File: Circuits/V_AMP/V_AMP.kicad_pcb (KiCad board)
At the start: 2 copper layers, 103.5 x 153.8 mm, 138 parts, among them P1 INPUT, P2 GAIN_ADJ, P3 OUTPUT (0-5V), P4 POWER, U1 OPA277, U2 LM393, U3 OPA277

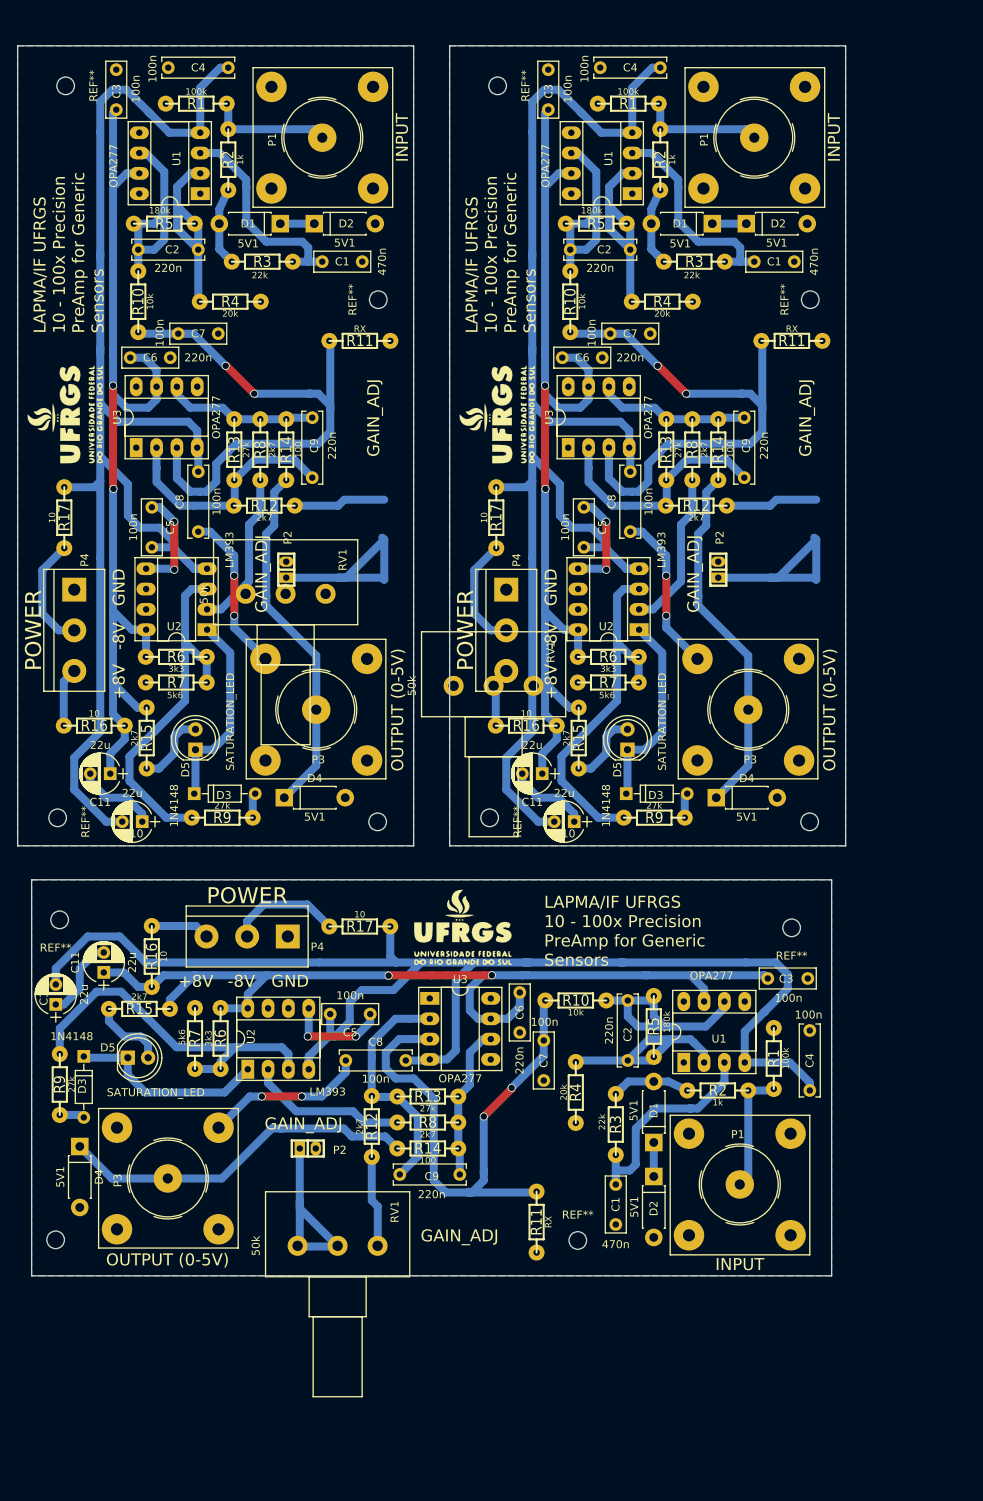
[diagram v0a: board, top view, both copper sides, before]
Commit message: EDIT: Shunt power resistors for alimentation input
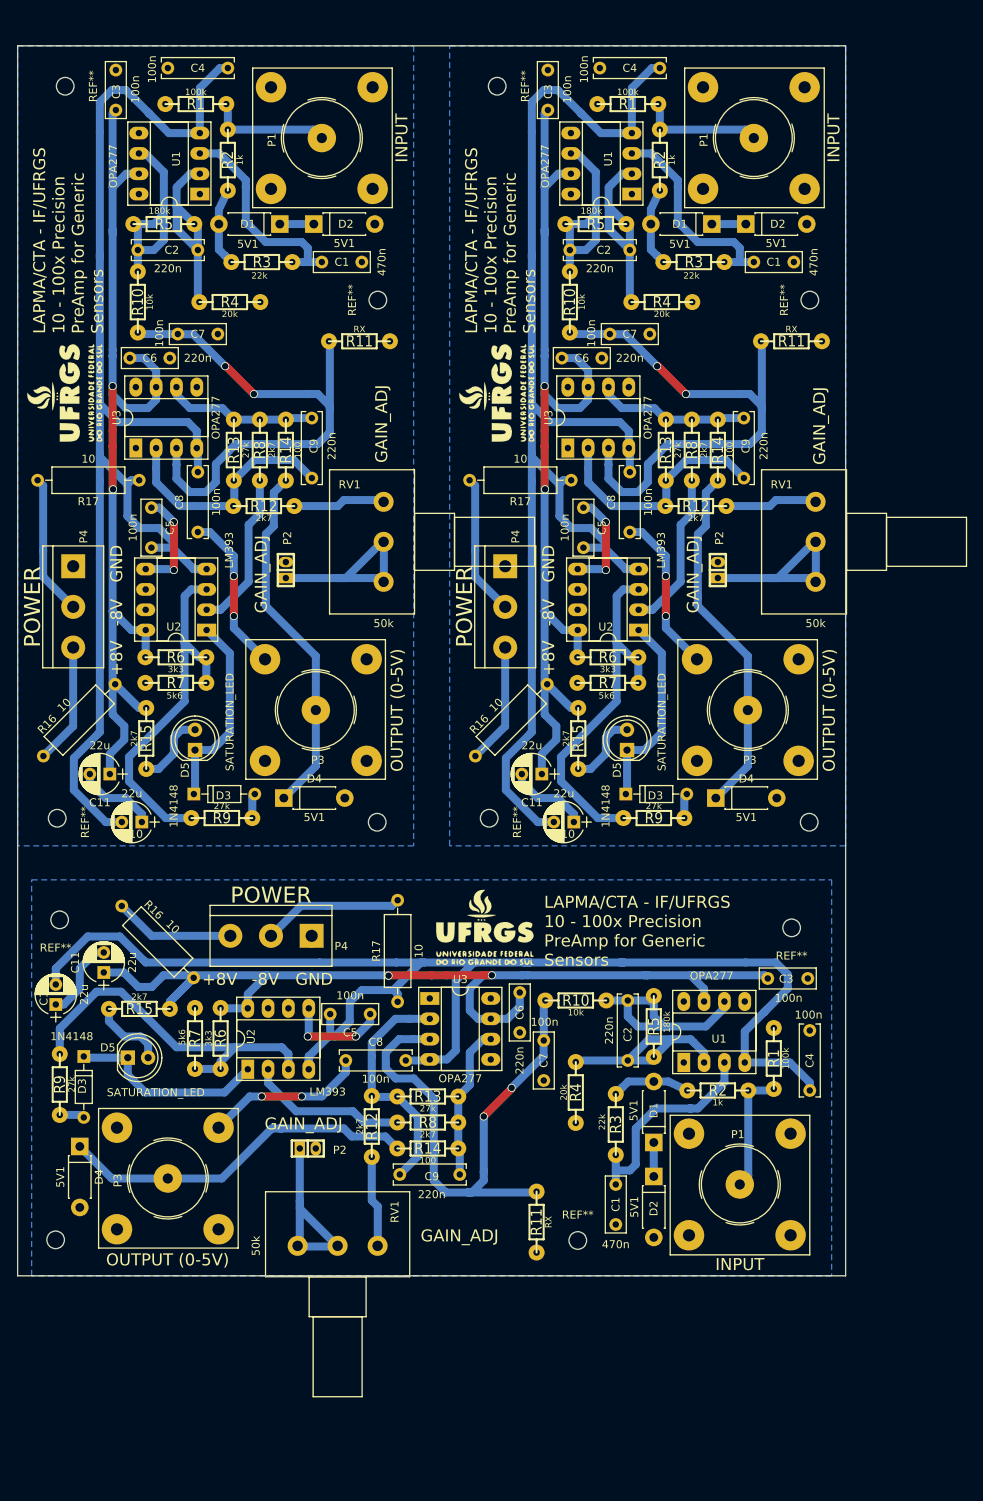
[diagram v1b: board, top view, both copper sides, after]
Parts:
- removed the C1 at (142.3, 59.7)
- removed the C1 at (88.3, 59.7)
- removed the C10 at (119.8, 129.7)
- removed the C10 at (65.8, 129.7)
- removed the C11 at (115.8, 123.7)
- removed the C11 at (61.8, 123.7)
- removed the C2 at (119.3, 58.2)
- removed the C2 at (65.3, 58.2)
- removed the C3 at (116.6, 35.7)
- removed the C3 at (62.6, 35.7)
- removed the C4 at (123.1, 35.5)
- removed the C4 at (69.1, 35.5)
- removed the C5 at (121.0, 90.4)
- removed the C5 at (67.0, 90.4)
- removed the C6 at (123.3, 71.7)
- removed the C6 at (69.3, 71.7)
- removed the C7 at (129.3, 68.7)
- removed the C7 at (75.3, 68.7)
- removed the C8 at (126.8, 93.5)
- removed the C8 at (72.8, 93.5)
- removed the C9 at (141.1, 86.7)
- removed the C9 at (87.1, 86.7)
- removed the D1 at (137.1, 55.0)
- removed the D1 at (83.1, 55.0)
- removed the D2 at (141.3, 55.0)
- removed the D2 at (87.3, 55.0)
- removed the D3 at (126.3, 126.2)
- removed the D3 at (72.3, 126.2)
- removed the D4 at (137.6, 126.7)
- removed the D4 at (83.6, 126.7)
- removed the D5 at (126.5, 120.7)
- removed the D5 at (72.5, 120.7)
- removed the G*** at (110.2, 78.8)
- removed the G*** at (56.2, 78.8)
- removed the P1 at (142.3, 44.2)
- removed the P1 at (88.3, 44.2)
- removed the P2 at (137.8, 98.2)
- removed the P2 at (83.8, 98.2)
- removed the P3 at (141.6, 115.7)
- removed the P3 at (87.6, 115.7)
- removed the P4 at (111.3, 100.7)
- removed the P4 at (57.3, 100.7)
- removed the R1 at (126.6, 40.0)
- removed the R1 at (72.6, 40.0)
- removed the R10 at (119.3, 64.7)
- removed the R10 at (65.3, 64.7)
- removed the R11 at (147.0, 69.6)
- removed the R11 at (93.0, 69.6)
- removed the R12 at (135.1, 90.2)
- removed the R12 at (81.1, 90.2)
- removed the R13 at (131.3, 83.2)
- removed the R13 at (77.3, 83.2)
- removed the R14 at (137.8, 83.2)
- removed the R14 at (83.8, 83.2)
- removed the R15 at (120.4, 119.3)
- removed the R15 at (66.4, 119.3)
- removed the R16 at (113.8, 117.7)
- removed the R16 at (59.8, 117.7)
- removed the R17 at (110.1, 91.7)
- removed the R17 at (56.1, 91.7)
- removed the R2 at (130.6, 47.0)
- removed the R2 at (76.6, 47.0)
- removed the R3 at (134.8, 59.7)
- removed the R3 at (80.8, 59.7)
- removed the R4 at (130.8, 64.7)
- removed the R4 at (76.8, 64.7)
- removed the R5 at (122.6, 55.0)
- removed the R5 at (68.6, 55.0)
- removed the R6 at (124.1, 109.1)
- removed the R6 at (70.1, 109.1)
- removed the R7 at (124.1, 112.3)
- removed the R7 at (70.1, 112.3)
- removed the R8 at (134.6, 83.2)
- removed the R8 at (80.6, 83.2)
- removed the R9 at (129.8, 129.2)
- removed the R9 at (75.8, 129.2)
- removed the REF** at (110.2, 37.8)
- removed the REF** at (149.3, 64.5)
- removed the REF** at (149.2, 129.8)
- removed the REF** at (109.2, 129.2)
- removed the REF** at (55.2, 129.2)
- removed the REF** at (95.2, 129.8)
- removed the REF** at (95.3, 64.5)
- removed the REF** at (56.2, 37.8)
- removed the RV1 at (104.8, 112.8)
- removed the RV1 at (78.8, 101.2)
- removed the U1 at (127.1, 51.2)
- removed the U1 at (73.1, 51.2)
- removed the U2 at (127.9, 105.7)
- removed the U2 at (73.9, 105.7)
- removed the U3 at (119.1, 83.0)
- removed the U3 at (65.1, 83.0)
- added C1: 470n, Capacitors_THT:C_Rect_L7.0mm_W2.5mm_P5.00mm, F.Cu at (88.3, 59.8)
- added C1: 470n, Capacitors_THT:C_Rect_L7.0mm_W2.5mm_P5.00mm, F.Cu at (142.3, 59.8)
- added C10: 22u, Capacitors_THT:CP_Radial_D5.0mm_P2.50mm, F.Cu at (65.8, 129.8)
- added C10: 22u, Capacitors_THT:CP_Radial_D5.0mm_P2.50mm, F.Cu at (119.8, 129.8)
- added C11: 22u, Capacitors_THT:CP_Radial_D5.0mm_P2.50mm, F.Cu at (61.8, 123.8)
- added C11: 22u, Capacitors_THT:CP_Radial_D5.0mm_P2.50mm, F.Cu at (115.8, 123.8)
- added C2: 220n, Capacitors_THT:C_Rect_L9.0mm_W2.5mm_P7.50mm_MKT, F.Cu at (65.3, 58.3)
- added C2: 220n, Capacitors_THT:C_Rect_L9.0mm_W2.5mm_P7.50mm_MKT, F.Cu at (119.3, 58.3)
- added C3: 100n, Capacitors_THT:C_Rect_L7.0mm_W2.5mm_P5.00mm, F.Cu at (62.5, 35.8)
- added C3: 100n, Capacitors_THT:C_Rect_L7.0mm_W2.5mm_P5.00mm, F.Cu at (116.5, 35.8)
- added C4: 100n, Capacitors_THT:C_Rect_L9.0mm_W2.5mm_P7.50mm_MKT, F.Cu at (69.0, 35.5)
- added C4: 100n, Capacitors_THT:C_Rect_L9.0mm_W2.5mm_P7.50mm_MKT, F.Cu at (123.0, 35.5)
- added C5: 100n, Capacitors_THT:C_Rect_L7.0mm_W2.5mm_P5.00mm, F.Cu at (67.0, 90.5)
- added C5: 100n, Capacitors_THT:C_Rect_L7.0mm_W2.5mm_P5.00mm, F.Cu at (121.0, 90.5)
- added C6: 100n, Capacitors_THT:C_Rect_L7.0mm_W2.5mm_P5.00mm, F.Cu at (69.3, 71.8)
- added C6: 100n, Capacitors_THT:C_Rect_L7.0mm_W2.5mm_P5.00mm, F.Cu at (123.3, 71.8)
- added C7: 220n, Capacitors_THT:C_Rect_L7.0mm_W2.5mm_P5.00mm, F.Cu at (75.3, 68.8)
- added C7: 220n, Capacitors_THT:C_Rect_L7.0mm_W2.5mm_P5.00mm, F.Cu at (129.3, 68.8)
- added C8: 100n, Capacitors_THT:C_Rect_L9.0mm_W2.5mm_P7.50mm_MKT, F.Cu at (72.8, 93.5)
- added C8: 100n, Capacitors_THT:C_Rect_L9.0mm_W2.5mm_P7.50mm_MKT, F.Cu at (126.8, 93.5)
- added C9: 220n, Capacitors_THT:C_Rect_L9.0mm_W2.5mm_P7.50mm_MKT, F.Cu at (87.0, 86.8)
- added C9: 220n, Capacitors_THT:C_Rect_L9.0mm_W2.5mm_P7.50mm_MKT, F.Cu at (141.0, 86.8)
- added D1: 5V1, Diodes_THT:D_DO-41_SOD81_P7.62mm_Horizontal, F.Cu at (83.0, 55.0)
- added D1: 5V1, Diodes_THT:D_DO-41_SOD81_P7.62mm_Horizontal, F.Cu at (137.0, 55.0)
- added D2: 5V1, Diodes_THT:D_DO-41_SOD81_P7.62mm_Horizontal, F.Cu at (87.3, 55.0)
- added D2: 5V1, Diodes_THT:D_DO-41_SOD81_P7.62mm_Horizontal, F.Cu at (141.3, 55.0)
- added D3: 1N4148, Diodes_THT:D_DO-35_SOD27_P7.62mm_Horizontal, F.Cu at (72.3, 126.3)
- added D3: 1N4148, Diodes_THT:D_DO-35_SOD27_P7.62mm_Horizontal, F.Cu at (126.3, 126.3)
- added D4: 5V1, Diodes_THT:D_DO-41_SOD81_P7.62mm_Horizontal, F.Cu at (83.5, 126.8)
- added D4: 5V1, Diodes_THT:D_DO-41_SOD81_P7.62mm_Horizontal, F.Cu at (137.5, 126.8)
- added D5: SATURATION_LED, LEDs:LED_D5.0mm, F.Cu at (72.4, 120.8)
- added D5: SATURATION_LED, LEDs:LED_D5.0mm, F.Cu at (126.4, 120.8)
- added G***: LOGO, Symbols:ufrgs, F.Cu at (56.2, 76.0)
- added G***: LOGO, Symbols:ufrgs, F.Cu at (110.2, 76.0)
- added P1: INPUT, Connectors:bnc-ci, F.Cu at (88.3, 44.3)
- added P1: INPUT, Connectors:bnc-ci, F.Cu at (142.3, 44.3)
- added P2: GAIN_ADJ, w_pin_strip:pin_strip_2mm_2, F.Cu at (83.8, 98.3)
- added P2: GAIN_ADJ, w_pin_strip:pin_strip_2mm_2, F.Cu at (137.8, 98.3)
- added P3: OUTPUT (0-5V), Connectors:bnc-ci, F.Cu at (87.5, 115.8)
- added P3: OUTPUT (0-5V), Connectors:bnc-ci, F.Cu at (141.5, 115.8)
- added P4: POWER, Connectors:bornier3, F.Cu at (57.2, 97.8)
- added P4: POWER, Connectors:bornier3, F.Cu at (111.2, 97.8)
- added R1: 100k, w_pth_resistors:RC03, F.Cu at (72.5, 40.0)
- added R1: 100k, w_pth_resistors:RC03, F.Cu at (126.5, 40.0)
- added R10: 10k, w_pth_resistors:RC03, F.Cu at (65.3, 64.8)
- added R10: 10k, w_pth_resistors:RC03, F.Cu at (119.3, 64.8)
- added R11: RX, w_pth_resistors:RC03, F.Cu at (93.0, 69.7)
- added R11: RX, w_pth_resistors:RC03, F.Cu at (147.0, 69.7)
- added R12: 2k7, w_pth_resistors:RC03, F.Cu at (81.0, 90.3)
- added R12: 2k7, w_pth_resistors:RC03, F.Cu at (135.0, 90.3)
- added R13: 27k, w_pth_resistors:RC03, F.Cu at (77.3, 83.3)
- added R13: 27k, w_pth_resistors:RC03, F.Cu at (131.3, 83.3)
- added R14: 100, w_pth_resistors:RC03, F.Cu at (83.8, 83.3)
- added R14: 100, w_pth_resistors:RC03, F.Cu at (137.8, 83.3)
- added R15: 2k7, w_pth_resistors:RC03, F.Cu at (66.3, 119.3)
- added R15: 2k7, w_pth_resistors:RC03, F.Cu at (120.3, 119.3)
- added R16: 10, Resistors_THT:R_Axial_DIN0309_L9.0mm_D3.2mm_P12.70mm_Horizontal, F.Cu at (62.4, 112.5)
- added R16: 10, Resistors_THT:R_Axial_DIN0309_L9.0mm_D3.2mm_P12.70mm_Horizontal, F.Cu at (116.4, 112.5)
- added R17: 10, Resistors_THT:R_Axial_DIN0309_L9.0mm_D3.2mm_P12.70mm_Horizontal, F.Cu at (65.4, 87.0)
- added R17: 10, Resistors_THT:R_Axial_DIN0309_L9.0mm_D3.2mm_P12.70mm_Horizontal, F.Cu at (119.4, 87.0)
- added R2: 1k, w_pth_resistors:RC03, F.Cu at (76.5, 47.0)
- added R2: 1k, w_pth_resistors:RC03, F.Cu at (130.5, 47.0)
- added R3: 22k, w_pth_resistors:RC03, F.Cu at (80.8, 59.8)
- added R3: 22k, w_pth_resistors:RC03, F.Cu at (134.8, 59.8)
- added R4: 20k, w_pth_resistors:RC03, F.Cu at (76.8, 64.8)
- added R4: 20k, w_pth_resistors:RC03, F.Cu at (130.8, 64.8)
- added R5: 180k, w_pth_resistors:RC03, F.Cu at (68.5, 55.0)
- added R5: 180k, w_pth_resistors:RC03, F.Cu at (122.5, 55.0)
- added R6: 3k3, w_pth_resistors:RC03, F.Cu at (70.0, 109.2)
- added R6: 3k3, w_pth_resistors:RC03, F.Cu at (124.0, 109.2)
- added R7: 5k6, w_pth_resistors:RC03, F.Cu at (70.0, 112.4)
- added R7: 5k6, w_pth_resistors:RC03, F.Cu at (124.0, 112.4)
- added R8: 2k7, w_pth_resistors:RC03, F.Cu at (80.5, 83.3)
- added R8: 2k7, w_pth_resistors:RC03, F.Cu at (134.5, 83.3)
- added R9: 27k, w_pth_resistors:RC03, F.Cu at (75.8, 129.3)
- added R9: 27k, w_pth_resistors:RC03, F.Cu at (129.8, 129.3)
- added REF**: MountingHole_2.2mm_M2, Mounting_Holes:MountingHole_2.2mm_M2, F.Cu at (56.2, 37.8)
- added REF**: MountingHole_2.2mm_M2, Mounting_Holes:MountingHole_2.2mm_M2, F.Cu at (95.3, 64.5)
- added REF**: MountingHole_2.2mm_M2, Mounting_Holes:MountingHole_2.2mm_M2, F.Cu at (95.2, 129.8)
- added REF**: MountingHole_2.2mm_M2, Mounting_Holes:MountingHole_2.2mm_M2, F.Cu at (55.2, 129.3)
- added REF**: MountingHole_2.2mm_M2, Mounting_Holes:MountingHole_2.2mm_M2, F.Cu at (109.2, 129.3)
- added REF**: MountingHole_2.2mm_M2, Mounting_Holes:MountingHole_2.2mm_M2, F.Cu at (149.2, 129.8)
- added REF**: MountingHole_2.2mm_M2, Mounting_Holes:MountingHole_2.2mm_M2, F.Cu at (149.3, 64.5)
- added REF**: MountingHole_2.2mm_M2, Mounting_Holes:MountingHole_2.2mm_M2, F.Cu at (110.2, 37.8)
- added RV1: 50k, Potentiometers:Potentiometer_Alps_RK163_Single_Vertical, F.Cu at (96.0, 99.8)
- added RV1: 50k, Potentiometers:Potentiometer_Alps_RK163_Single_Vertical, F.Cu at (150.0, 99.8)
- added U1: OPA277, Housings_DIP:DIP-8_W7.62mm_Socket_LongPads, F.Cu at (73.0, 51.3)
- added U1: OPA277, Housings_DIP:DIP-8_W7.62mm_Socket_LongPads, F.Cu at (127.0, 51.3)
- added U2: LM393, Housings_DIP:DIP-8_W7.62mm_Socket_LongPads, F.Cu at (73.9, 105.8)
- added U2: LM393, Housings_DIP:DIP-8_W7.62mm_Socket_LongPads, F.Cu at (127.9, 105.8)
- added U3: OPA277, Housings_DIP:DIP-8_W7.62mm_Socket_LongPads, F.Cu at (65.0, 83.0)
- added U3: OPA277, Housings_DIP:DIP-8_W7.62mm_Socket_LongPads, F.Cu at (119.0, 83.0)
- R16, R17: footprint w_pth_resistors:RC03 -> Resistors_THT:R_Axial_DIN0309_L9.0mm_D3.2mm_P12.70mm_Horizontal
- moved R17 10.5 mm to (97.8, 152.2), turned to 90 degrees
- moved R16 5.87 mm to (72.2, 149.2), turned to 135 degrees
- moved P4 2.98 mm to (87.0, 144.0)
- moved G*** 2.75 mm to (108.8, 143.0)
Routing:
- net Net-(P4-Pad3): track 16.1 -> 46.7 mm
- net +8V: track 355.5 -> 366.1 mm
- net Net-(P4-Pad2): track 45.6 -> 56.0 mm
- net -8V: track 519.1 -> 509.7 mm
- net Net-(P2-Pad1): track 83.7 -> 76.3 mm
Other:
- outline, holes or cut-outs redrawn
- board text added: "LAPMA/CTA - IF/UFRGS 10 - 100x Precision PreAmp for Generic Sensors"
- board text removed: "LAPMA/IF UFRGS 10 - 100x Precision PreAmp for Generic Sensors"

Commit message: ADD: Complete Current Source SCH+PCB w/ Gerbers
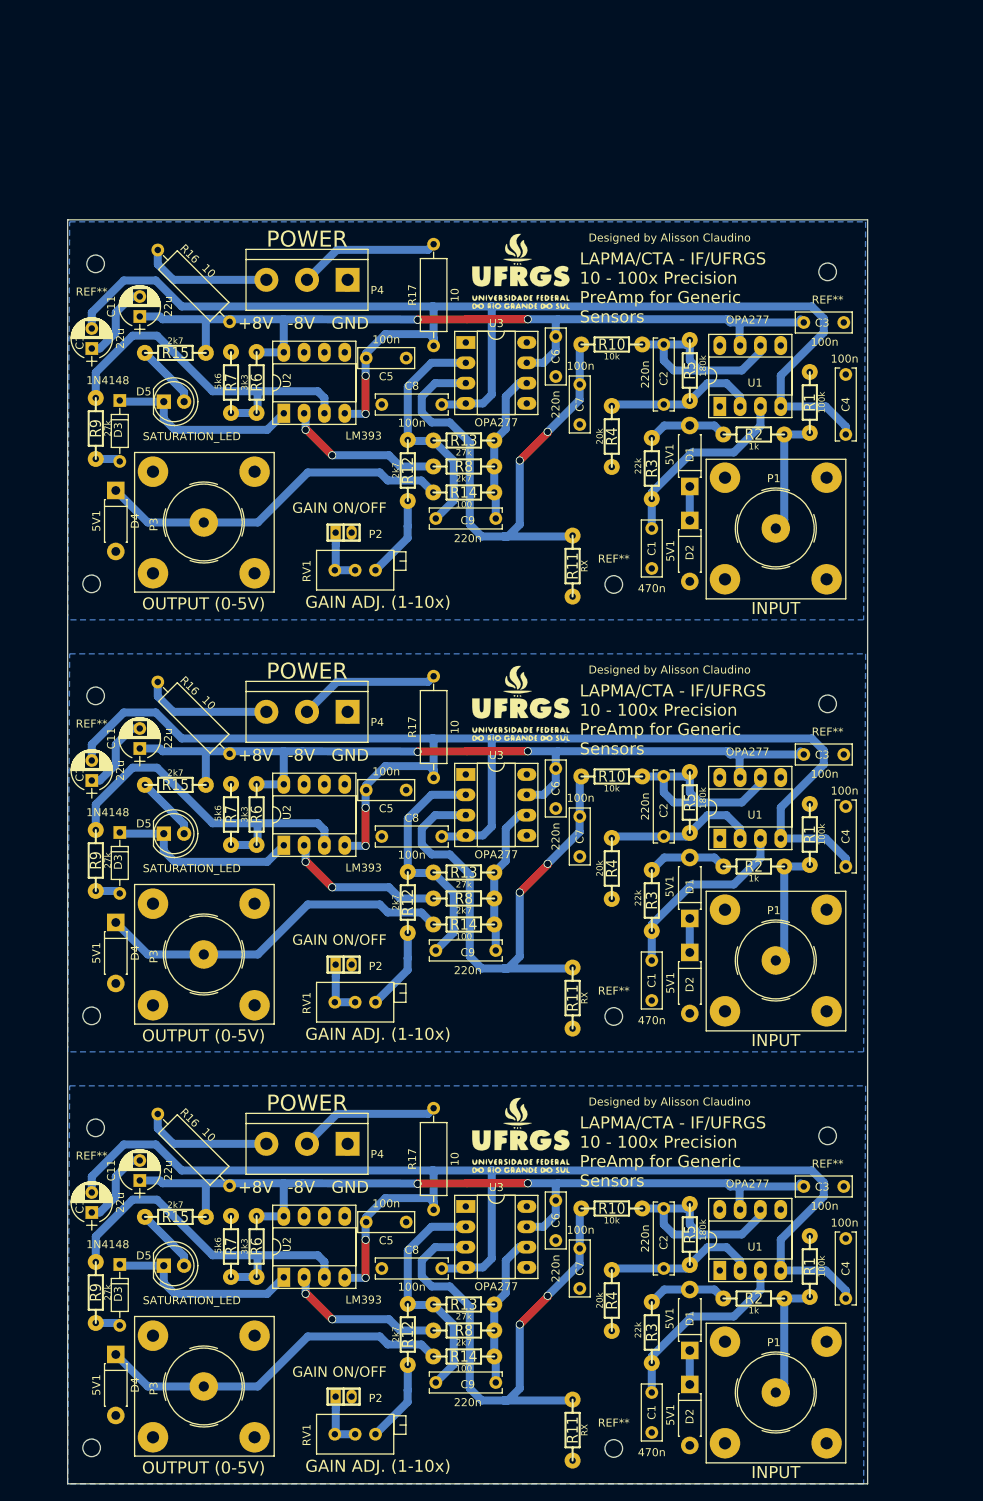
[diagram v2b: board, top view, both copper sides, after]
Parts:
- removed the C1 at (88.3, 59.8)
- removed the C1 at (142.3, 59.8)
- removed the C10 at (65.8, 129.8)
- removed the C10 at (119.8, 129.8)
- removed the C11 at (61.8, 123.8)
- removed the C11 at (115.8, 123.8)
- removed the C2 at (65.3, 58.3)
- removed the C2 at (119.3, 58.3)
- removed the C3 at (62.5, 35.8)
- removed the C3 at (116.5, 35.8)
- removed the C4 at (69.0, 35.5)
- removed the C4 at (123.0, 35.5)
- removed the C5 at (67.0, 90.5)
- removed the C5 at (121.0, 90.5)
- removed the C6 at (69.3, 71.8)
- removed the C6 at (123.3, 71.8)
- removed the C7 at (75.3, 68.8)
- removed the C7 at (129.3, 68.8)
- removed the C8 at (72.8, 93.5)
- removed the C8 at (126.8, 93.5)
- removed the C9 at (87.0, 86.8)
- removed the C9 at (141.0, 86.8)
- removed the D1 at (83.0, 55.0)
- removed the D1 at (137.0, 55.0)
- removed the D2 at (87.3, 55.0)
- removed the D2 at (141.3, 55.0)
- removed the D3 at (72.3, 126.3)
- removed the D3 at (126.3, 126.3)
- removed the D4 at (83.5, 126.8)
- removed the D4 at (137.5, 126.8)
- removed the D5 at (72.4, 120.8)
- removed the D5 at (126.4, 120.8)
- removed the G*** at (56.2, 76.0)
- removed the G*** at (110.2, 76.0)
- removed the P1 at (88.3, 44.3)
- removed the P1 at (142.3, 44.3)
- removed the P2 at (83.8, 98.3)
- removed the P2 at (137.8, 98.3)
- removed the P3 at (87.5, 115.8)
- removed the P3 at (141.5, 115.8)
- removed the P4 at (57.2, 97.8)
- removed the P4 at (111.2, 97.8)
- removed the R1 at (72.5, 40.0)
- removed the R1 at (126.5, 40.0)
- removed the R10 at (65.3, 64.8)
- removed the R10 at (119.3, 64.8)
- removed the R11 at (93.0, 69.7)
- removed the R11 at (147.0, 69.7)
- removed the R12 at (81.0, 90.3)
- removed the R12 at (135.0, 90.3)
- removed the R13 at (77.3, 83.3)
- removed the R13 at (131.3, 83.3)
- removed the R14 at (83.8, 83.3)
- removed the R14 at (137.8, 83.3)
- removed the R15 at (66.3, 119.3)
- removed the R15 at (120.3, 119.3)
- removed the R16 at (62.4, 112.5)
- removed the R16 at (116.4, 112.5)
- removed the R17 at (65.4, 87.0)
- removed the R17 at (119.4, 87.0)
- removed the R2 at (76.5, 47.0)
- removed the R2 at (130.5, 47.0)
- removed the R3 at (80.8, 59.8)
- removed the R3 at (134.8, 59.8)
- removed the R4 at (76.8, 64.8)
- removed the R4 at (130.8, 64.8)
- removed the R5 at (68.5, 55.0)
- removed the R5 at (122.5, 55.0)
- removed the R6 at (70.0, 109.2)
- removed the R6 at (124.0, 109.2)
- removed the R7 at (70.0, 112.4)
- removed the R7 at (124.0, 112.4)
- removed the R8 at (80.5, 83.3)
- removed the R8 at (134.5, 83.3)
- removed the R9 at (75.8, 129.3)
- removed the R9 at (129.8, 129.3)
- removed the REF** at (56.2, 37.8)
- removed the REF** at (95.3, 64.5)
- removed the REF** at (95.2, 129.8)
- removed the REF** at (55.2, 129.3)
- removed the REF** at (109.2, 129.3)
- removed the REF** at (149.2, 129.8)
- removed the REF** at (149.3, 64.5)
- removed the REF** at (110.2, 37.8)
- removed the RV1 at (96.0, 99.8)
- removed the RV1 at (150.0, 99.8)
- removed the U1 at (73.0, 51.3)
- removed the U1 at (127.0, 51.3)
- removed the U2 at (73.9, 105.8)
- removed the U2 at (127.9, 105.8)
- removed the U3 at (65.0, 83.0)
- removed the U3 at (119.0, 83.0)
- added C1: 470n, Capacitors_THT:C_Rect_L7.0mm_W2.5mm_P5.00mm, F.Cu at (129.5, 93.1)
- added C1: 470n, Capacitors_THT:C_Rect_L7.0mm_W2.5mm_P5.00mm, F.Cu at (129.5, 147.1)
- added C10: 22u, Capacitors_THT:CP_Radial_D5.0mm_P2.50mm, F.Cu at (59.5, 70.6)
- added C10: 22u, Capacitors_THT:CP_Radial_D5.0mm_P2.50mm, F.Cu at (59.5, 124.6)
- added C11: 22u, Capacitors_THT:CP_Radial_D5.0mm_P2.50mm, F.Cu at (65.5, 66.6)
- added C11: 22u, Capacitors_THT:CP_Radial_D5.0mm_P2.50mm, F.Cu at (65.5, 120.6)
- added C2: 220n, Capacitors_THT:C_Rect_L9.0mm_W2.5mm_P7.50mm_MKT, F.Cu at (131.0, 70.1)
- added C2: 220n, Capacitors_THT:C_Rect_L9.0mm_W2.5mm_P7.50mm_MKT, F.Cu at (131.0, 124.1)
- added C3: 100n, Capacitors_THT:C_Rect_L7.0mm_W2.5mm_P5.00mm, F.Cu at (153.5, 67.3)
- added C3: 100n, Capacitors_THT:C_Rect_L7.0mm_W2.5mm_P5.00mm, F.Cu at (153.5, 121.3)
- added C4: 100n, Capacitors_THT:C_Rect_L9.0mm_W2.5mm_P7.50mm_MKT, F.Cu at (153.8, 73.8)
- added C4: 100n, Capacitors_THT:C_Rect_L9.0mm_W2.5mm_P7.50mm_MKT, F.Cu at (153.8, 127.8)
- added C5: 100n, Capacitors_THT:C_Rect_L7.0mm_W2.5mm_P5.00mm, F.Cu at (98.8, 71.8)
- added C5: 100n, Capacitors_THT:C_Rect_L7.0mm_W2.5mm_P5.00mm, F.Cu at (98.8, 125.8)
- added C6: 100n, Capacitors_THT:C_Rect_L7.0mm_W2.5mm_P5.00mm, F.Cu at (117.5, 74.1)
- added C6: 100n, Capacitors_THT:C_Rect_L7.0mm_W2.5mm_P5.00mm, F.Cu at (117.5, 128.1)
- added C7: 220n, Capacitors_THT:C_Rect_L7.0mm_W2.5mm_P5.00mm, F.Cu at (120.5, 80.1)
- added C7: 220n, Capacitors_THT:C_Rect_L7.0mm_W2.5mm_P5.00mm, F.Cu at (120.5, 134.1)
- added C8: 100n, Capacitors_THT:C_Rect_L9.0mm_W2.5mm_P7.50mm_MKT, F.Cu at (95.8, 77.6)
- added C8: 100n, Capacitors_THT:C_Rect_L9.0mm_W2.5mm_P7.50mm_MKT, F.Cu at (95.8, 131.6)
- added C9: 220n, Capacitors_THT:C_Rect_L9.0mm_W2.5mm_P7.50mm_MKT, F.Cu at (102.5, 91.8)
- added C9: 220n, Capacitors_THT:C_Rect_L9.0mm_W2.5mm_P7.50mm_MKT, F.Cu at (102.5, 145.8)
- added D1: 5V1, Diodes_THT:D_DO-41_SOD81_P7.62mm_Horizontal, F.Cu at (134.3, 87.8)
- added D1: 5V1, Diodes_THT:D_DO-41_SOD81_P7.62mm_Horizontal, F.Cu at (134.3, 141.8)
- added D2: 5V1, Diodes_THT:D_DO-41_SOD81_P7.62mm_Horizontal, F.Cu at (134.3, 92.1)
- added D2: 5V1, Diodes_THT:D_DO-41_SOD81_P7.62mm_Horizontal, F.Cu at (134.3, 146.1)
- added D3: 1N4148, Diodes_THT:D_DO-35_SOD27_P7.62mm_Horizontal, F.Cu at (63.0, 77.1)
- added D3: 1N4148, Diodes_THT:D_DO-35_SOD27_P7.62mm_Horizontal, F.Cu at (63.0, 131.1)
- added D4: 5V1, Diodes_THT:D_DO-41_SOD81_P7.62mm_Horizontal, F.Cu at (62.5, 88.3)
- added D4: 5V1, Diodes_THT:D_DO-41_SOD81_P7.62mm_Horizontal, F.Cu at (62.5, 142.3)
- added D5: SATURATION_LED, LEDs:LED_D5.0mm, F.Cu at (68.5, 77.2)
- added D5: SATURATION_LED, LEDs:LED_D5.0mm, F.Cu at (68.5, 131.2)
- added G***: LOGO, Symbols:ufrgs, F.Cu at (113.2, 61.0)
- added G***: LOGO, Symbols:ufrgs, F.Cu at (113.2, 115.0)
- added P1: INPUT, Connectors:bnc-ci, F.Cu at (145.0, 93.1)
- added P1: INPUT, Connectors:bnc-ci, F.Cu at (145.0, 147.1)
- added P2: GAIN ON/OFF, w_pin_strip:pin_strip_2mm_2, F.Cu at (91.0, 93.6)
- added P2: GAIN ON/OFF, w_pin_strip:pin_strip_2mm_2, F.Cu at (91.0, 147.6)
- added P3: OUTPUT (0-5V), Connectors:bnc-ci, F.Cu at (73.5, 92.3)
- added P3: OUTPUT (0-5V), Connectors:bnc-ci, F.Cu at (73.5, 146.3)
- added P4: POWER, Connectors:bornier3, F.Cu at (91.5, 62.0)
- added P4: POWER, Connectors:bornier3, F.Cu at (91.5, 116.0)
- added R1: 100k, w_pth_resistors:RC03, F.Cu at (149.3, 77.3)
- added R1: 100k, w_pth_resistors:RC03, F.Cu at (149.3, 131.3)
- added R10: 10k, w_pth_resistors:RC03, F.Cu at (124.5, 70.1)
- added R10: 10k, w_pth_resistors:RC03, F.Cu at (124.5, 124.1)
- added R11: RX, w_pth_resistors:RC03, F.Cu at (119.6, 97.8)
- added R11: RX, w_pth_resistors:RC03, F.Cu at (119.6, 151.8)
- added R12: 2k7, w_pth_resistors:RC03, F.Cu at (99.0, 85.8)
- added R12: 2k7, w_pth_resistors:RC03, F.Cu at (99.0, 139.8)
- added R13: 27k, w_pth_resistors:RC03, F.Cu at (106.0, 82.1)
- added R13: 27k, w_pth_resistors:RC03, F.Cu at (106.0, 136.1)
- added R14: 100, w_pth_resistors:RC03, F.Cu at (106.0, 88.6)
- added R14: 100, w_pth_resistors:RC03, F.Cu at (106.0, 142.6)
- added R15: 2k7, w_pth_resistors:RC03, F.Cu at (70.0, 71.1)
- added R15: 2k7, w_pth_resistors:RC03, F.Cu at (70.0, 125.1)
- added R16: 10, Resistors_THT:R_Axial_DIN0309_L9.0mm_D3.2mm_P12.70mm_Horizontal, F.Cu at (76.8, 67.2)
- added R16: 10, Resistors_THT:R_Axial_DIN0309_L9.0mm_D3.2mm_P12.70mm_Horizontal, F.Cu at (76.8, 121.2)
- added R17: 10, Resistors_THT:R_Axial_DIN0309_L9.0mm_D3.2mm_P12.70mm_Horizontal, F.Cu at (102.2, 70.2)
- added R17: 10, Resistors_THT:R_Axial_DIN0309_L9.0mm_D3.2mm_P12.70mm_Horizontal, F.Cu at (102.2, 124.2)
- added R2: 1k, w_pth_resistors:RC03, F.Cu at (142.3, 81.3)
- added R2: 1k, w_pth_resistors:RC03, F.Cu at (142.3, 135.3)
- added R3: 22k, w_pth_resistors:RC03, F.Cu at (129.5, 85.6)
- added R3: 22k, w_pth_resistors:RC03, F.Cu at (129.5, 139.6)
- added R4: 20k, w_pth_resistors:RC03, F.Cu at (124.5, 81.6)
- added R4: 20k, w_pth_resistors:RC03, F.Cu at (124.5, 135.6)
- added R5: 180k, w_pth_resistors:RC03, F.Cu at (134.3, 73.3)
- added R5: 180k, w_pth_resistors:RC03, F.Cu at (134.3, 127.3)
- added R6: 3k3, w_pth_resistors:RC03, F.Cu at (80.1, 74.8)
- added R6: 3k3, w_pth_resistors:RC03, F.Cu at (80.1, 128.8)
- added R7: 5k6, w_pth_resistors:RC03, F.Cu at (76.9, 74.8)
- added R7: 5k6, w_pth_resistors:RC03, F.Cu at (76.9, 128.8)
- added R8: 2k7, w_pth_resistors:RC03, F.Cu at (106.0, 85.3)
- added R8: 2k7, w_pth_resistors:RC03, F.Cu at (106.0, 139.3)
- added R9: 27k, w_pth_resistors:RC03, F.Cu at (60.0, 80.6)
- added R9: 27k, w_pth_resistors:RC03, F.Cu at (60.0, 134.6)
- added REF**: MountingHole_2.2mm_M2, Mounting_Holes:MountingHole_2.2mm_M2, F.Cu at (151.5, 61.0)
- added REF**: MountingHole_2.2mm_M2, Mounting_Holes:MountingHole_2.2mm_M2, F.Cu at (124.8, 100.1)
- added REF**: MountingHole_2.2mm_M2, Mounting_Holes:MountingHole_2.2mm_M2, F.Cu at (59.5, 100.0)
- added REF**: MountingHole_2.2mm_M2, Mounting_Holes:MountingHole_2.2mm_M2, F.Cu at (60.0, 60.0)
- added REF**: MountingHole_2.2mm_M2, Mounting_Holes:MountingHole_2.2mm_M2, F.Cu at (60.0, 114.0)
- added REF**: MountingHole_2.2mm_M2, Mounting_Holes:MountingHole_2.2mm_M2, F.Cu at (59.5, 154.0)
- added REF**: MountingHole_2.2mm_M2, Mounting_Holes:MountingHole_2.2mm_M2, F.Cu at (124.8, 154.1)
- added REF**: MountingHole_2.2mm_M2, Mounting_Holes:MountingHole_2.2mm_M2, F.Cu at (151.5, 115.0)
- added RV1: 50k, Potentiometers:Potentiometer_Trimmer_Bourns_3296X, F.Cu at (89.9, 98.3)
- added RV1: 50k, Potentiometers:Potentiometer_Trimmer_Bourns_3296X, F.Cu at (89.9, 152.3)
- added U1: OPA277, Housings_DIP:DIP-8_W7.62mm_Socket_LongPads, F.Cu at (138.0, 77.8)
- added U1: OPA277, Housings_DIP:DIP-8_W7.62mm_Socket_LongPads, F.Cu at (138.0, 131.8)
- added U2: LM393, Housings_DIP:DIP-8_W7.62mm_Socket_LongPads, F.Cu at (83.5, 78.7)
- added U2: LM393, Housings_DIP:DIP-8_W7.62mm_Socket_LongPads, F.Cu at (83.5, 132.7)
- added U3: OPA277, Housings_DIP:DIP-8_W7.62mm_Socket_LongPads, F.Cu at (106.3, 69.8)
- added U3: OPA277, Housings_DIP:DIP-8_W7.62mm_Socket_LongPads, F.Cu at (106.3, 123.8)
- P2: value GAIN_ADJ -> GAIN ON/OFF
- RV1: footprint Potentiometers:Potentiometer_Alps_RK163_Single_Vertical -> Potentiometers:Potentiometer_Trimmer_Bourns_3296X
- moved P2 31.3 mm to (91.0, 201.6)
- moved C1 26.4 mm to (129.5, 201.1)
- moved C2 26.4 mm to (131.0, 178.1)
- moved R3 26.4 mm to (129.5, 193.6)
- moved C10 26.4 mm to (59.5, 178.6)
- moved C11 26.4 mm to (65.5, 174.6)
- moved C3 26.4 mm to (153.5, 175.3)
- moved C4 26.4 mm to (153.8, 181.8)
- moved C5 26.4 mm to (98.8, 179.8)
- moved C6 26.4 mm to (117.5, 182.1)
- moved C7 26.4 mm to (120.5, 188.1)
- moved C8 26.4 mm to (95.8, 185.6)
- moved C9 26.4 mm to (102.5, 199.8)
- moved D1 26.4 mm to (134.3, 195.8)
- moved D2 26.4 mm to (134.3, 200.1)
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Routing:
- net GND: track 133.9 -> 33.8 mm, vias 12 -> 0
- net Net-(P2-Pad1): track 76.3 -> 22.1 mm
- net +8V: track 366.1 -> 321.4 mm
- net Net-(C2-Pad2): track 77.1 -> 57.4 mm
- net -8V: track 509.7 -> 492.7 mm, vias 0 -> 6
- net Net-(C1-Pad1): track 82.0 -> 71.9 mm
- net Net-(D5-Pad2): track 28.0 -> 24.4 mm
- net Net-(P4-Pad3): track 46.7 -> 49.8 mm
- net Net-(R12-Pad2): track 34.5 -> 32.1 mm
- net Net-(R6-Pad2): track 136.4 -> 134.3 mm
- net Net-(D3-Pad1): track 74.5 -> 72.4 mm
- net Net-(C7-Pad2): track 204.2 -> 203.5 mm
- net Net-(D4-Pad1): track 135.7 -> 134.9 mm
- net Net-(R8-Pad1): track 59.8 -> 60.0 mm, vias 0 -> 6
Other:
- board size 103.5 x 153.8 mm -> 100 x 158 mm
- board text added: "Designed by Alisson Claudino"
- board text added: "GAIN ADJ. (1-10x)"
- board text removed: "GAIN_ADJ"
